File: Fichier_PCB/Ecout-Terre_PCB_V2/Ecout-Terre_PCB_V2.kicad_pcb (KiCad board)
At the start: 4 copper layers, 92 x 86 mm, 111 parts, among them J1 USB_C_Receptacle_USB2.0, J10 Micro_SD_Card, J11 Test_10V, J12 Conn_test_ampli, J13 Conn_GPS, J14 AudioJack_Mono, J2 Pile, J4 Test_5V, J5 Conn_Alim, J6 Test_3V3, J7 Conn_ESP, J8 Conn_ESP, J9 Sortie_alim, Q1 CSD16327Q3, U1 TS3480CX33RFG, U2 MC33269, U3 LM3478, U4 PCM1804, U5 TL072, U6 LM386, U7 74LVT04, Y1 7V-22.5792MAHV-T

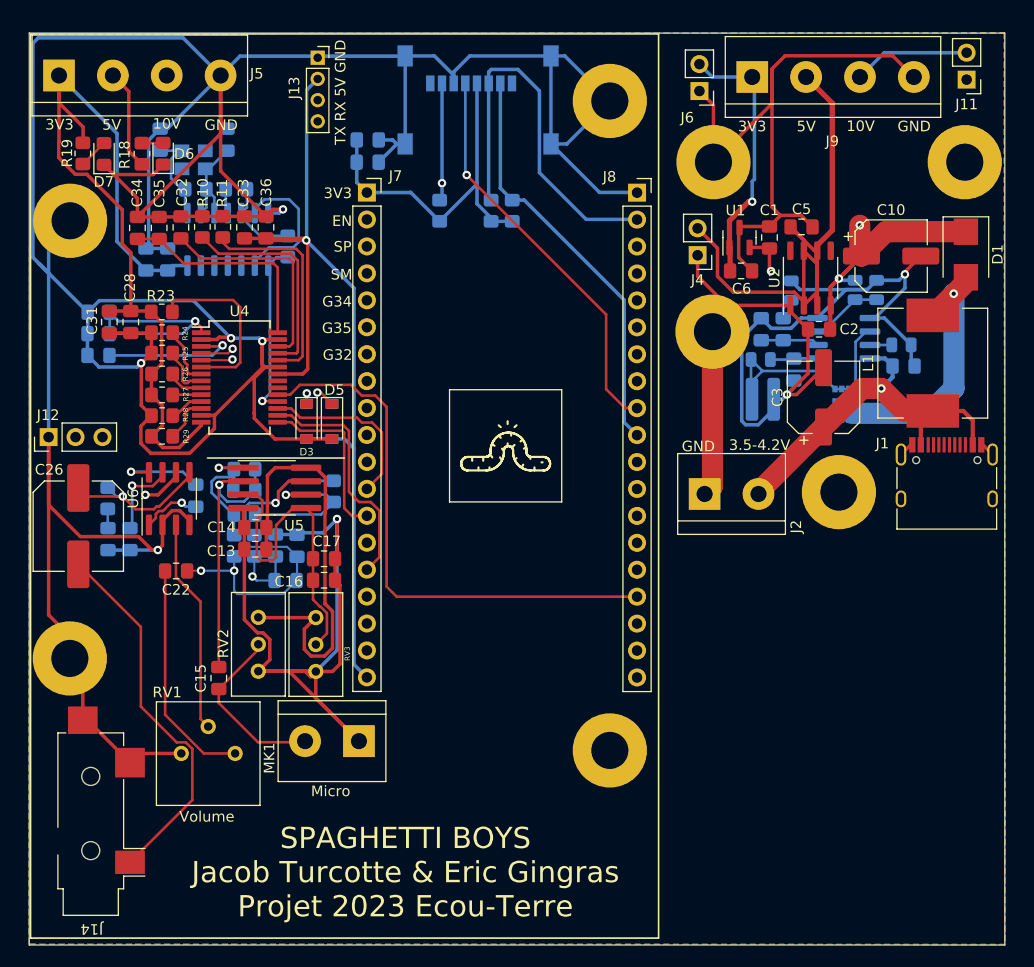
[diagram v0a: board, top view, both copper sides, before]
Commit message: Trace pcb
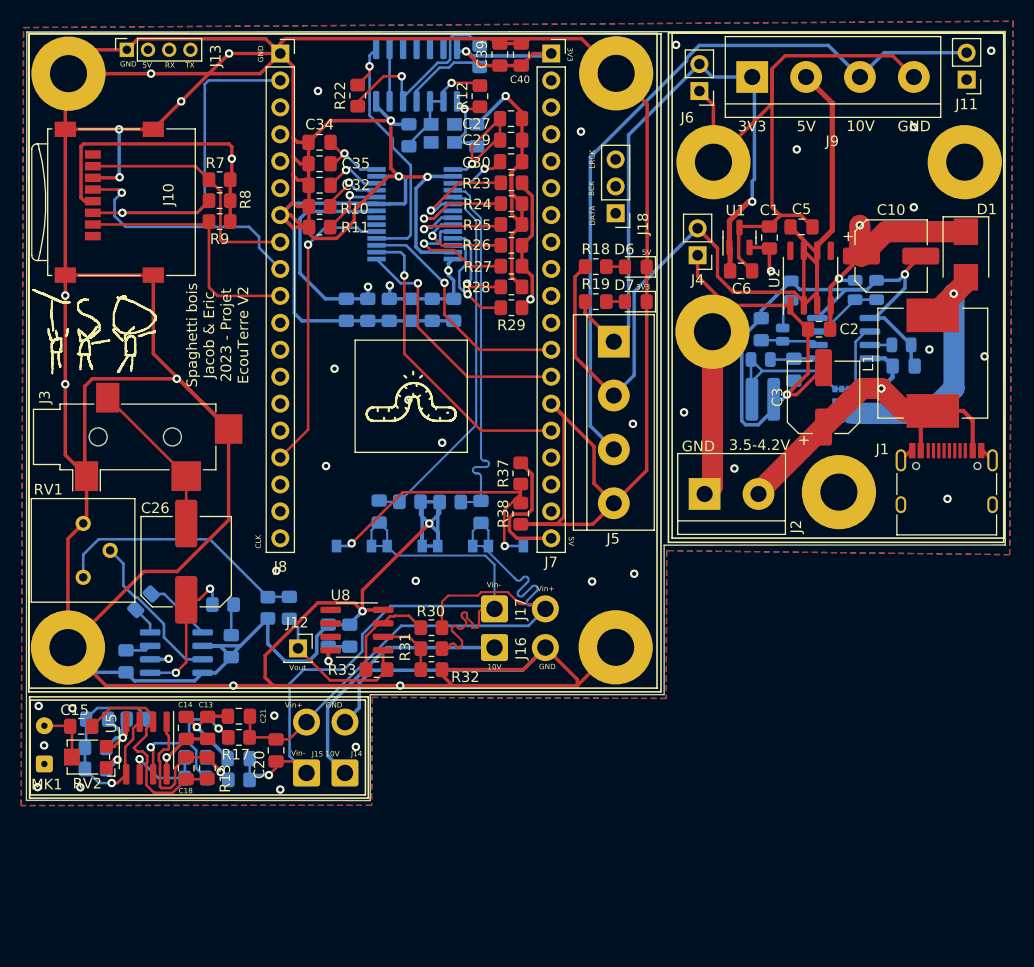
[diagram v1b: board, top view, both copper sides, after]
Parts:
- removed the ? at (114.3, 125.5)
- removed the ? at (114.3, 84.2)
- removed the ? at (165.2, 134.2)
- removed the ? at (165.2, 72.9)
- removed RV3: 100k, Potentiometer_THT:Potentiometer_Bourns_3296W_Vertical
- added ?: , , F.Cu at (114.2, 70.3)
- added ?: , , F.Cu at (165.8, 124.4)
- added ?: , , F.Cu at (165.8, 70.3)
- added ?: , , F.Cu at (114.2, 124.5)
- added C41: 1uF, Capacitor_SMD:C_0805_2012Metric_Pad1.18x1.45mm_HandSolder, B.Cu at (138.7, 123.3)
- added C42: 0.1uF, Capacitor_SMD:C_0805_2012Metric_Pad1.18x1.45mm_HandSolder, B.Cu at (140.7, 123.3)
- added C43: 1uF, Capacitor_SMD:C_0805_2012Metric_Pad1.18x1.45mm_HandSolder, B.Cu at (143.5, 111.6)
- added C44: 1uF, Capacitor_SMD:C_0805_2012Metric_Pad1.18x1.45mm_HandSolder, B.Cu at (153.1, 111.7)
- added J15: Conn_Audio_Diff, Connector_Wire:SolderWire-0.75sqmm_1x02_P4.8mm_D1.25mm_OD2.3mm, F.Cu at (136.7, 136.3)
- added J16: Conn_Main_Alim, Connector_Wire:SolderWire-0.75sqmm_1x02_P4.8mm_D1.25mm_OD2.3mm, F.Cu at (154.4, 124.5)
- added J17: Conn_Main_Diff, Connector_Wire:SolderWire-0.75sqmm_1x02_P4.8mm_D1.25mm_OD2.3mm, F.Cu at (154.4, 120.8)
- added J18: Conn_01x03_Male, Connector_PinHeader_2.54mm:PinHeader_1x03_P2.54mm_Vertical, F.Cu at (165.8, 83.5)
- added J3: AudioJack4, Connector_Audio:Jack_3.5mm_CUI_SJ-3524-SMT_Horizontal, F.Cu at (119.5, 104.6)
- added R30: 10k, Resistor_SMD:R_0805_2012Metric_Pad1.20x1.40mm_HandSolder, F.Cu at (148.4, 122.6)
- added R31: 10k, Resistor_SMD:R_0805_2012Metric_Pad1.20x1.40mm_HandSolder, F.Cu at (148.4, 124.5)
- added R32: 10k, Resistor_SMD:R_0805_2012Metric_Pad1.20x1.40mm_HandSolder, F.Cu at (148.4, 126.5)
- added R33: 10k, Resistor_SMD:R_0805_2012Metric_Pad1.20x1.40mm_HandSolder, F.Cu at (143.2, 126.5)
- added R34: 2.2k, Resistor_SMD:R_0805_2012Metric_Pad1.20x1.40mm_HandSolder, B.Cu at (146.4, 110.7)
- added R35: 2.2k, Resistor_SMD:R_0805_2012Metric_Pad1.20x1.40mm_HandSolder, B.Cu at (150.2, 110.7)
- added R36: 680, Resistor_SMD:R_0805_2012Metric_Pad1.20x1.40mm_HandSolder, B.Cu at (133.0, 120.7)
- added R37: 10k, Resistor_SMD:R_0805_2012Metric_Pad1.20x1.40mm_HandSolder, F.Cu at (156.8, 108.0)
- added R38: 10k, Resistor_SMD:R_0805_2012Metric_Pad1.20x1.40mm_HandSolder, F.Cu at (156.8, 111.8)
- added R39: 9.1k, Resistor_SMD:R_0805_2012Metric_Pad1.20x1.40mm_HandSolder, B.Cu at (116.8, 135.9)
- added R40: 1.25k, Resistor_SMD:R_0805_2012Metric_Pad1.20x1.40mm_HandSolder, B.Cu at (116.8, 133.9)
- added U8: OPA1656, Package_SO:SOIC-8_3.9x4.9mm_P1.27mm, F.Cu at (141.4, 122.8)
- C16, C17, C22, C28, C31, C33, C36, U4, U6: moved to B.Cu
- C18, C20, C27, C29, C30, C39, C40, J10, R12, R13, R22, R7, R8, R9: moved to F.Cu
- C19: value 100pF -> 0.022uF
- C21: value 100pF -> 0.022uF; moved to F.Cu
- C4: value 100nF -> 0.1uF
- C7: value 3.3nF -> 3300pF
- C8: footprint Capacitor_SMD:C_0805_2012Metric_Pad1.18x1.45mm_HandSolder -> Capacitor_SMD:C_0504_1310Metric_Pad0.83x1.28mm_HandSolder
- D2, D4: value D_Zener -> D_Z_2V4
- D3, D5: value D_Zener -> D_Z_2V4; moved to B.Cu
- J12: value Conn_test_ampli -> Conn_01x01_Male; footprint Connector_PinHeader_2.54mm:PinHeader_1x03_P2.54mm_Vertical -> Connector_PinSocket_2.54mm:PinSocket_1x01_P2.54mm_Vertical
- J14: value AudioJack_Mono -> Conn_Audio_Alim; footprint Audio:3_5mm_audioJack -> Connector_Wire:SolderWire-0.75sqmm_1x02_P4.8mm_D1.25mm_OD2.3mm
- MK1: footprint TerminalBlock:TerminalBlock_bornier-2_P5.08mm -> Connector_Wire:SolderWire-0.1sqmm_1x02_P3.6mm_D0.4mm_OD1mm
- R15: value 51 -> 120
- R17: value 51 -> 120; moved to F.Cu
- R4: value 7k -> 6.8k
- RV2: footprint Potentiometer_THT:Potentiometer_Bourns_3296W_Vertical -> Potentiometer_SMD:Potentiometer_Bourns_TC33X_Vertical
- U5: value TL072 -> OPA1656; footprint Custom_SOIC:SOIC-8_3.9_et_5.3mm -> Package_SO:SOIC-8_3.9x4.9mm_P1.27mm
- moved J5 58.0 mm to (165.6, 95.6), turned to -90 degrees
- moved D7 52.0 mm to (167.7, 91.8), turned to 180 degrees
- moved R19 50.4 mm to (163.9, 91.8), turned to 0 degrees
- moved D6 45.8 mm to (167.7, 88.5), turned to 180 degrees
- moved R18 44.1 mm to (163.9, 88.5), turned to 0 degrees
- moved C27 43.9 mm to (155.9, 74.6), turned to 0 degrees
- moved C30 43.0 mm to (155.9, 78.6), turned to 0 degrees
- moved C29 42.1 mm to (155.9, 76.6), turned to 180 degrees
- moved C39 38.6 mm to (154.9, 68.5)
- moved C40 38.5 mm to (156.9, 68.5)
- moved J8 36.1 mm to (134.2, 68.4)
- moved J10 36.1 mm to (118.0, 82.5), turned to 90 degrees
- moved R23 35.1 mm to (156.0, 80.6), turned to 180 degrees
- moved R24 35.1 mm to (156.0, 82.6), turned to 180 degrees
- moved R27 35.1 mm to (156.0, 88.5), turned to 180 degrees
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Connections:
- C19 pad 1: Vin- -> VinA-
- C20 pad 1: Vin+ -> VinA+
- C20 pad 2: Vin- -> VinA-
- C21 pad 2: Vin+ -> VinA+
- C22 pad 1: Vin- -> Vout
- D2 pad 1: 5V -> 2V5
- D2 pad 2: Vin- -> VinA-
- D3 pad 1: Vin- -> VinA-
- D4 pad 1: 5V -> 2V5
- D4 pad 2: Vin+ -> VinA+
- D5 pad 1: Vin+ -> VinA+
- J12 pad 1: GND -> Vout
- R15 pad 2: Vin- -> VinA-
- R17 pad 2: Vin+ -> VinA+
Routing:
- net GND: track 1052.8 -> 1501.0 mm, vias 8 -> 49
- net VinA-: track 0.00 -> 76.1 mm, vias 0 -> 1
- net VinA+: track 0.00 -> 68.6 mm
- net 10V: track 253.6 -> 308.9 mm, vias 4 -> 7
- net BCK: track 22.7 -> 70.7 mm, vias 0 -> 1
- net Vin-: track 77.2 -> 35.2 mm, vias 4 -> 0
- net 3V3: track 254.2 -> 292.0 mm, vias 1 -> 6
- net 5V: track 256.4 -> 289.6 mm
- net Vin+: track 68.3 -> 35.1 mm, vias 3 -> 0
- net /ESP-32/TX0: track 43.1 -> 11.8 mm
- net 2V5: track 0.00 -> 28.6 mm, vias 0 -> 2
- net LRCK: track 16.7 -> 42.8 mm, vias 0 -> 1
- net DATA: track 16.2 -> 41.4 mm, vias 0 -> 1
- net RST: track 52.5 -> 28.4 mm, vias 0 -> 1
- net /ESP-32/RX0: track 37.9 -> 14.8 mm
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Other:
- board size 92 x 86 mm -> 92.3 x 72.5 mm
- board text added: "BCK"
- board text added: "CLK"
- board text added: "DATA"
- board text added: "LRCK"
- board text added: "RX"
- board text added: "Spaghetti bois Jacob & Eric 2023 - Projet EcouTerre V2"
- board text added: "TX"
- board text added: "Vin+"
- board text added: "Vin-"
- board text added: "Vout"
- board text removed: "EN"
- board text removed: "G32"
- board text removed: "G34"
- board text removed: "G35"
- board text removed: "Micro"
- board text removed: "SM"
- board text removed: "SP"
- board text removed: "SPAGHETTI BOYS Jacob Turcotte & Eric Gingras Projet 2023 Ecou-Terre"
- board text removed: "TX RX 5V GND"
- board text removed: "Volume"
